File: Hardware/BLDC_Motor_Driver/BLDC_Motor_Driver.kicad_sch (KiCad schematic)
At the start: 0 parts

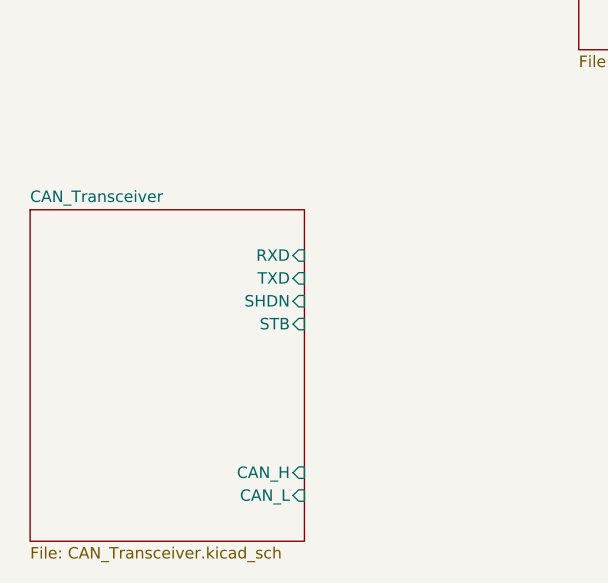
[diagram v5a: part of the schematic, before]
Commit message: add CS series resistor to EEPROM Schematic
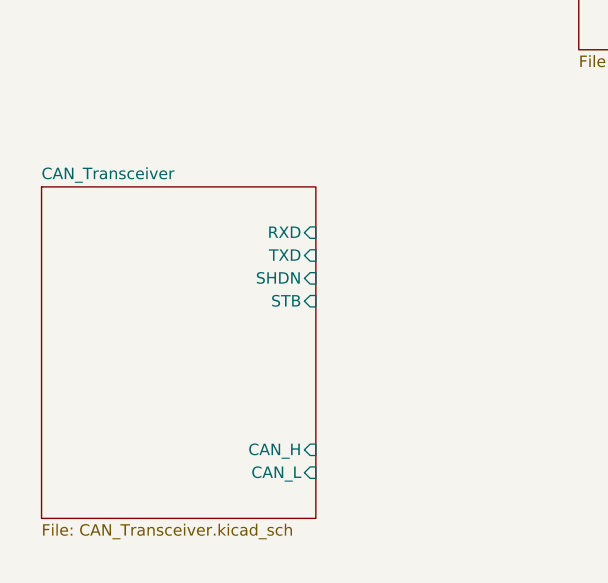
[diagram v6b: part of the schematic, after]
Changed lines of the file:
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@@
 	)
 	(sheet
-		(at 43.18 121.92)
+		(at 44.45 119.38)
 		(size 30.48 36.83)
 		(exclude_from_sim no)
@@
 		)
 		(property "Sheetname" "CAN_Transceiver"
-			(at 43.18 121.2084 0)
+			(at 44.45 118.6684 0)
 			(effects
 				(font
@@
 		)
 		(property "Sheetfile" "CAN_Transceiver.kicad_sch"
-			(at 43.18 159.3346 0)
+			(at 44.45 156.7946 0)
 			(effects
 				(font
@@
 		)
 		(pin "CAN_L" input
-			(at 73.66 153.67 0)
+			(at 74.93 151.13 0)
 			(effects
 				(font
@@
 		)
 		(pin "CAN_H" input
-			(at 73.66 151.13 0)
+			(at 74.93 148.59 0)
 			(effects
 				(font
@@
 		)
 		(pin "RXD" input
-			(at 73.66 127 0)
+			(at 74.93 124.46 0)
 			(effects
 				(font
@@
 		)
 		(pin "TXD" input
-			(at 73.66 129.54 0)
+			(at 74.93 127 0)
 			(effects
 				(font
@@
 		)
 		(pin "SHDN" input
-			(at 73.66 132.08 0)
+			(at 74.93 129.54 0)
 			(effects
 				(font
@@
 		)
 		(pin "STB" input
-			(at 73.66 134.62 0)
+			(at 74.93 132.08 0)
 			(effects
 				(font

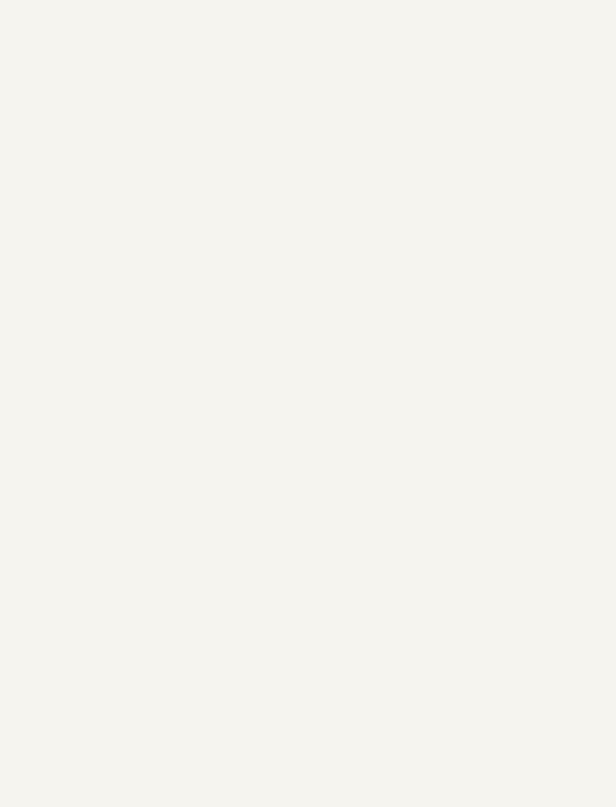
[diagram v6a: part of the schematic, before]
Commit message: Add the MOSFET for the 3 phase inverter sheet
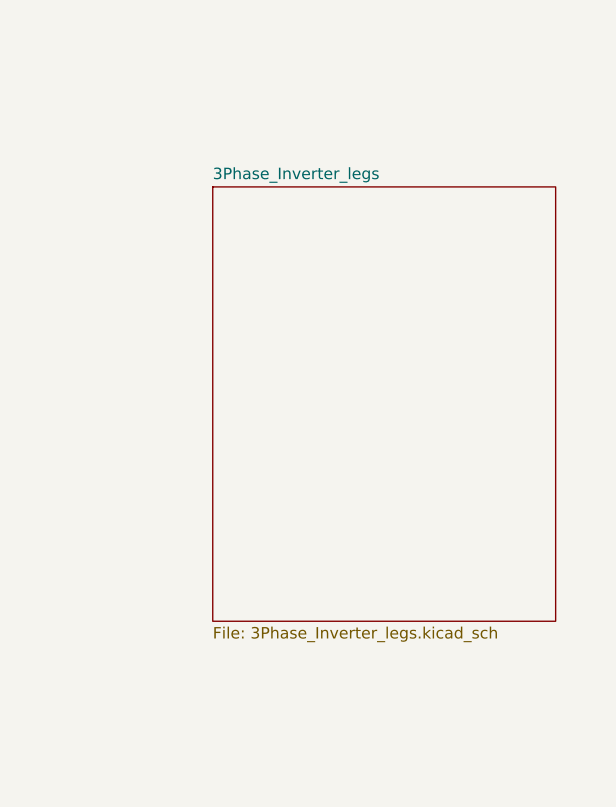
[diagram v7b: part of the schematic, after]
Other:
- added sheet 3Phase_Inverter_legs (3Phase_Inverter_legs.kicad_sch)
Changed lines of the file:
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@@
+	)
+	(sheet
+		(at 217.17 81.28)
+		(size 38.1 48.26)
+		(exclude_from_sim no)
+		(in_bom yes)
+		(on_board yes)
+		(dnp no)
+		(fields_autoplaced yes)
+		(stroke
+			(width 0.1524)
+			(type solid)
+		)
+		(fill
+			(color 0 0 0 0.0000)
+		)
+		(property "Sheetname" "3Phase_Inverter_legs"
+			(at 217.17 80.5684 0)
+			(effects
+				(font
+					(size 1.27 1.27)
+				)
+				(justify left bottom)
+			)
+		)
+		(property "Sheetfile" "3Phase_Inverter_legs.kicad_sch"
+			(at 217.17 130.1246 0)
+			(effects
+				(font
+					(size 1.27 1.27)
+				)
+				(justify left top)
+			)
+		)
+		(instances
+			(project "BLDC_Motor_Driver"
+				(path "/e34fda66-7244-4ac9-bbf7-3725f03e688f"
+					(page "6")
+				)
+			)
+		)
 	)
 	(sheet
